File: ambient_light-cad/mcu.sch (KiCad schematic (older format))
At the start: 24 parts

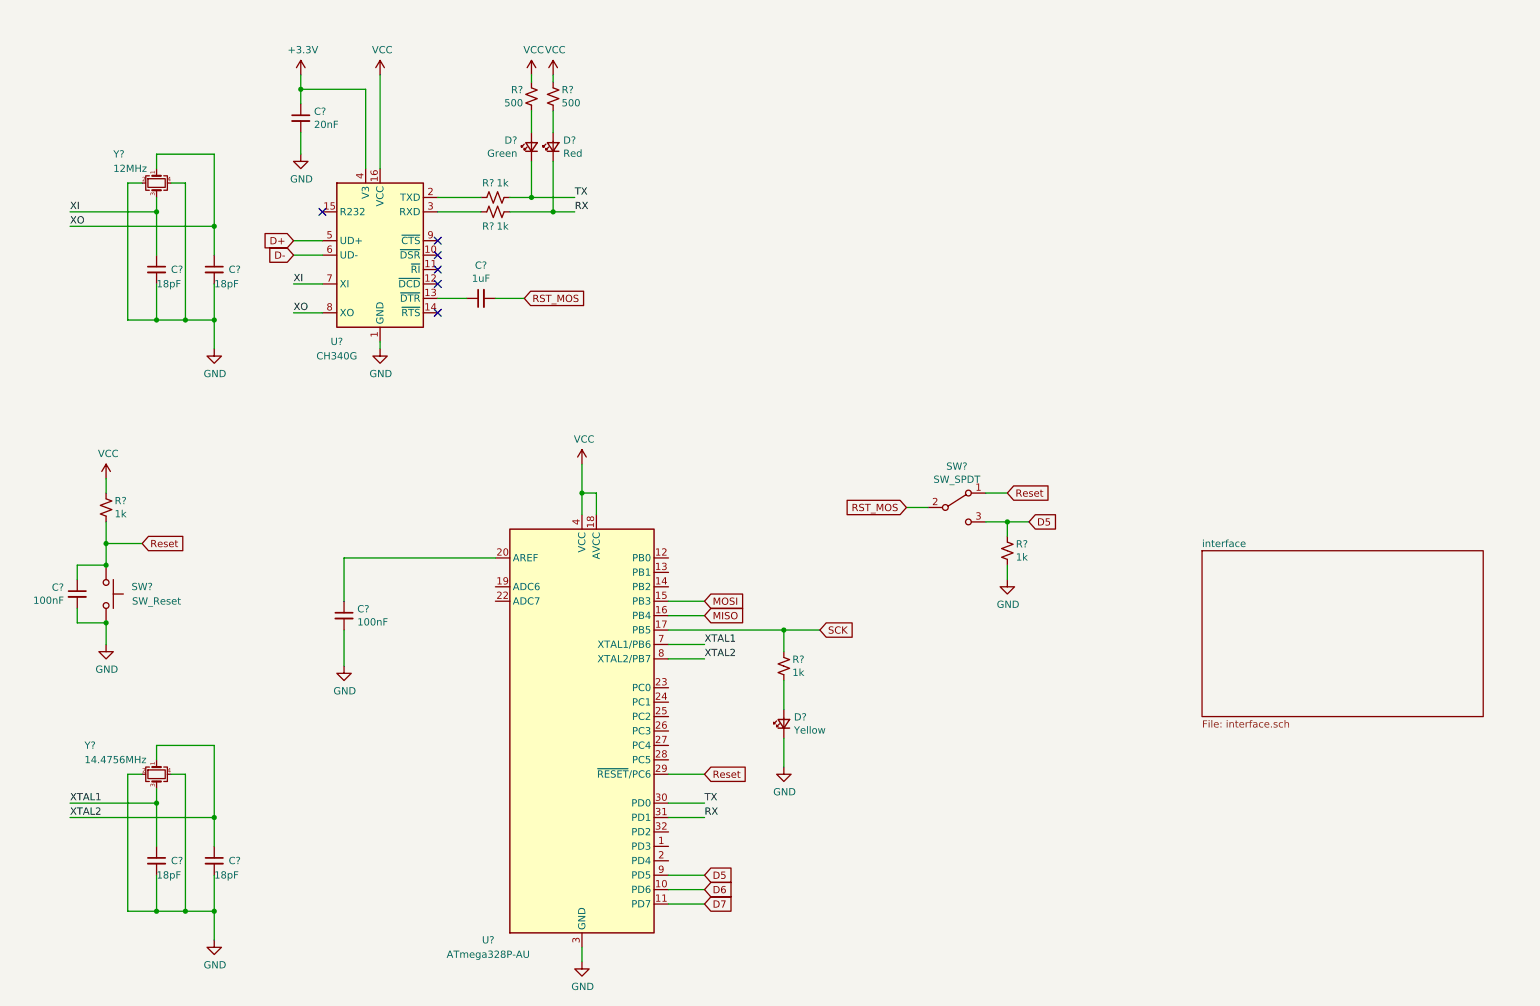
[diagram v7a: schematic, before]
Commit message: [Added] Test Point
RST, XTAL, USB Data
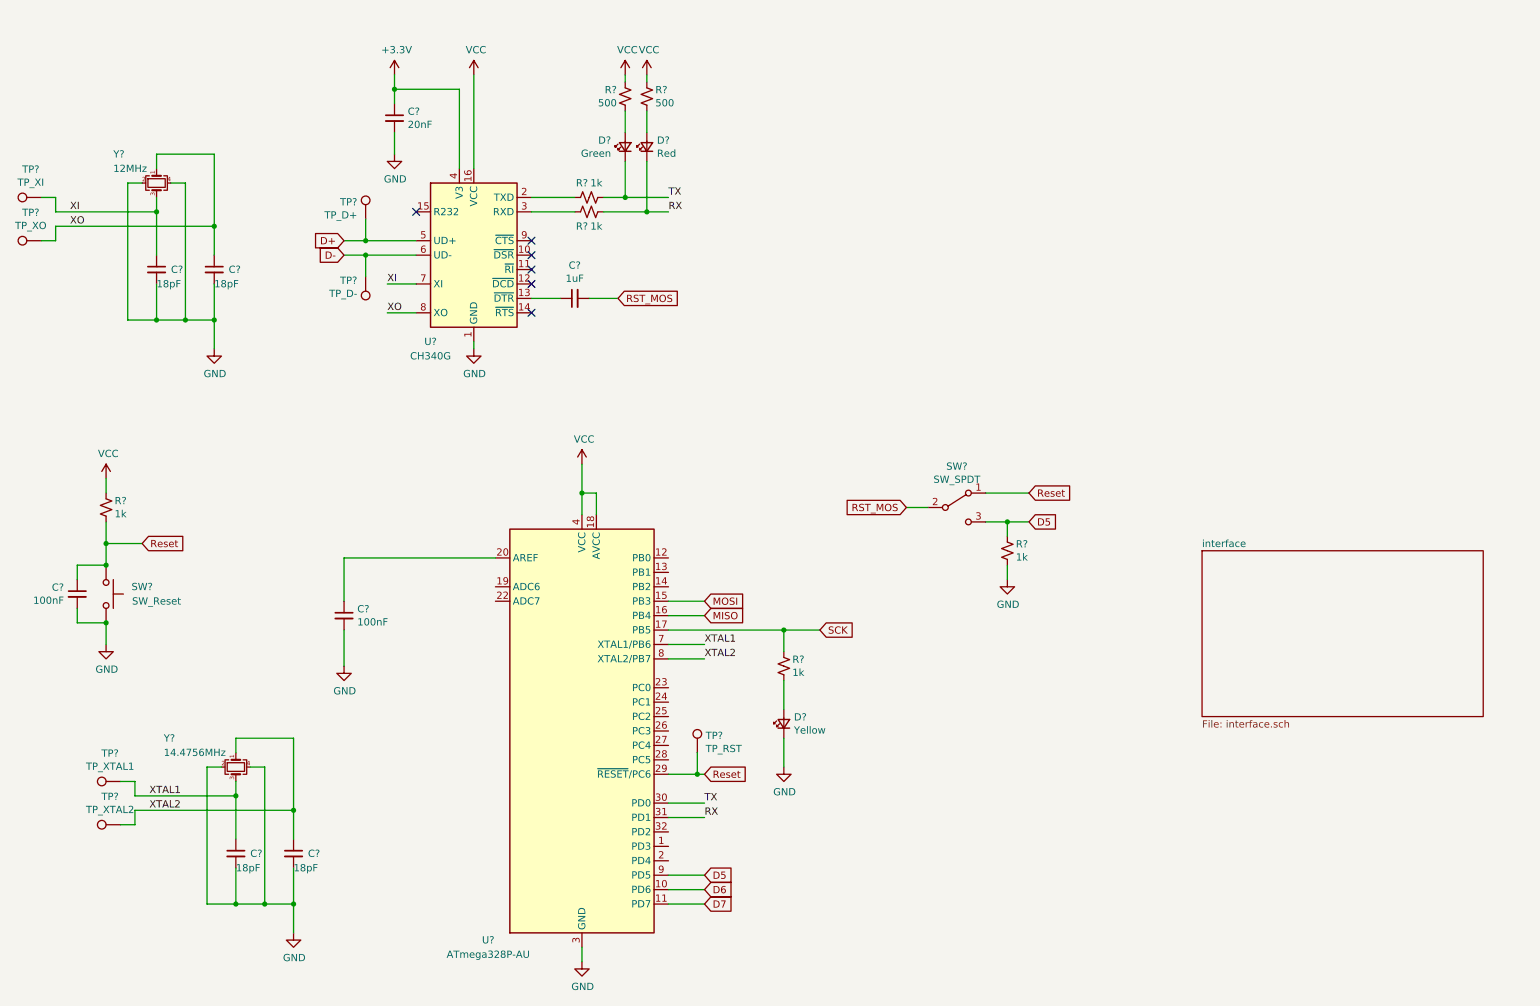
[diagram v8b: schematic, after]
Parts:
- added TP?: TP_XTAL1, symbol Connector:TestPoint
- added TP?: TP_XTAL2, symbol Connector:TestPoint
- added TP?: TP_XI, symbol Connector:TestPoint
- added TP?: TP_XO, symbol Connector:TestPoint
- added TP?: TP_RST, symbol Connector:TestPoint
- added TP?: TP_D+, symbol Connector:TestPoint
- added TP?: TP_D-, symbol Connector:TestPoint
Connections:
- net D+: now also TP?.1
- net D-: now also TP?.1
- net Reset: now also TP?.1
- net XI: now also TP?.1
- net XO: now also TP?.1
- net XTAL1: now also TP?.1
- net XTAL2: now also TP?.1
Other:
- moved on the sheet: C?, D?, R?, U?, Y?
